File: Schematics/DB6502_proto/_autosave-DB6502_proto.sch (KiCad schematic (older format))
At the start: 13 parts, among them U1 74HC21, U2 74AC74, U3 65C02S, U4 22V10C, U5 74AC138, U6 74AC08

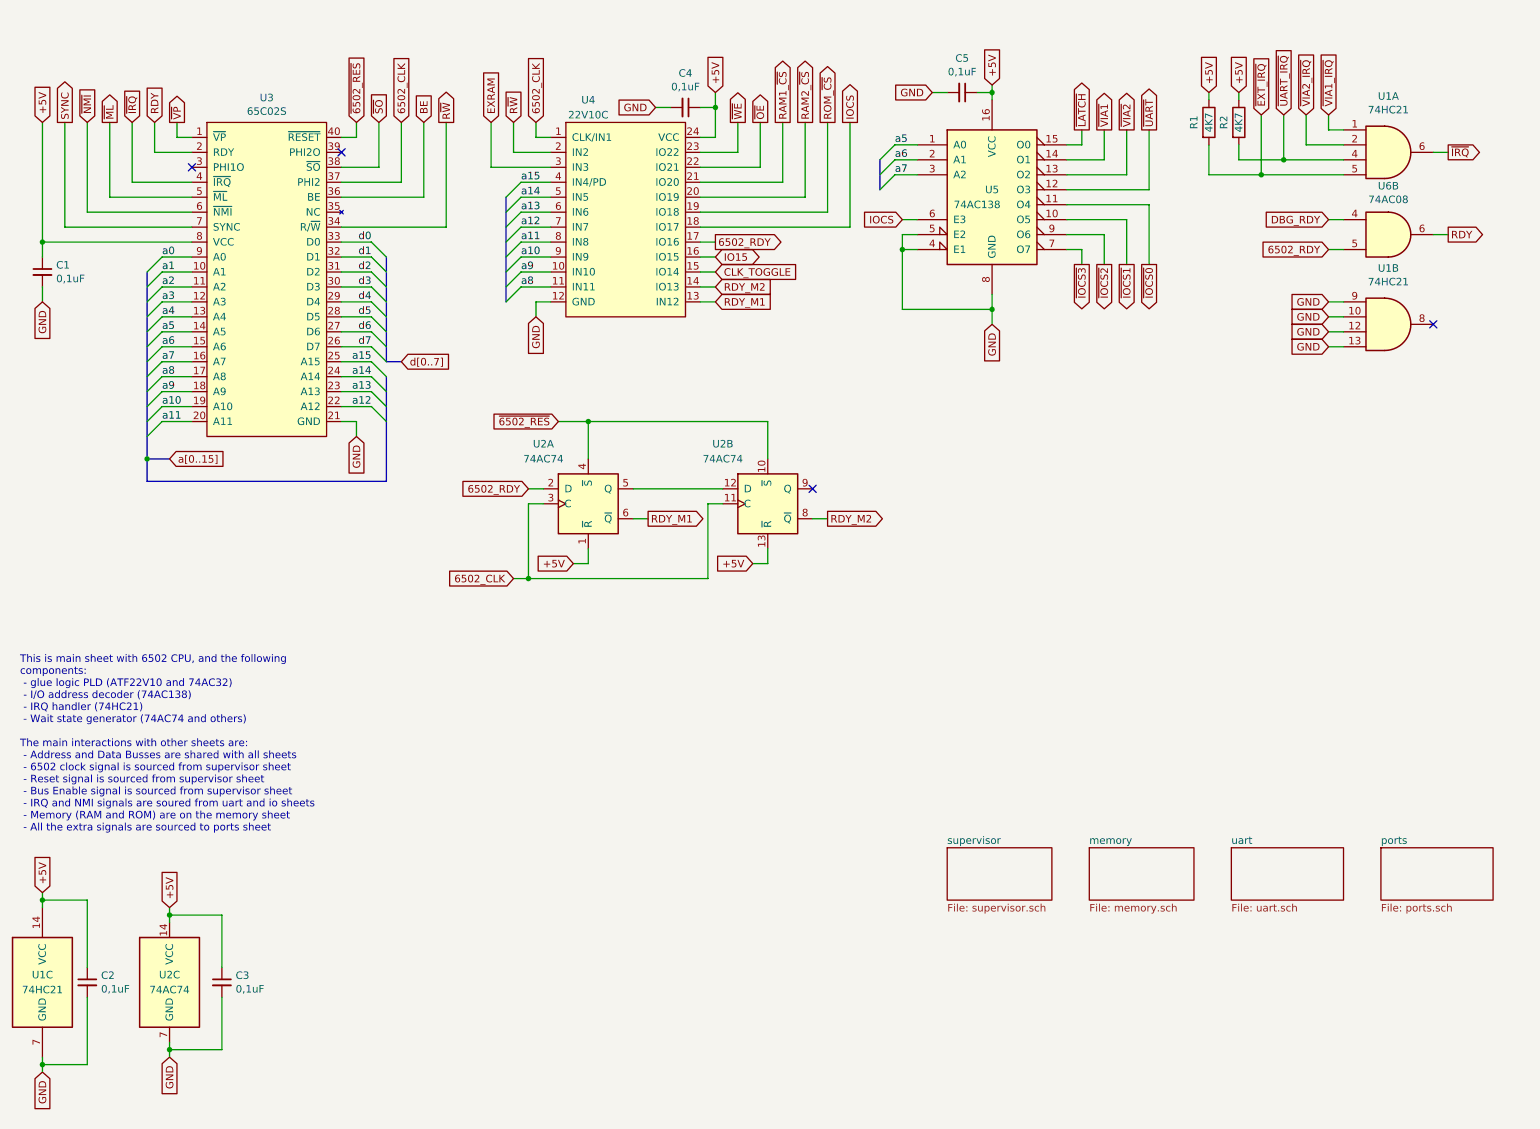
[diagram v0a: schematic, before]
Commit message: Updated schematic to reflect PLD WS generator
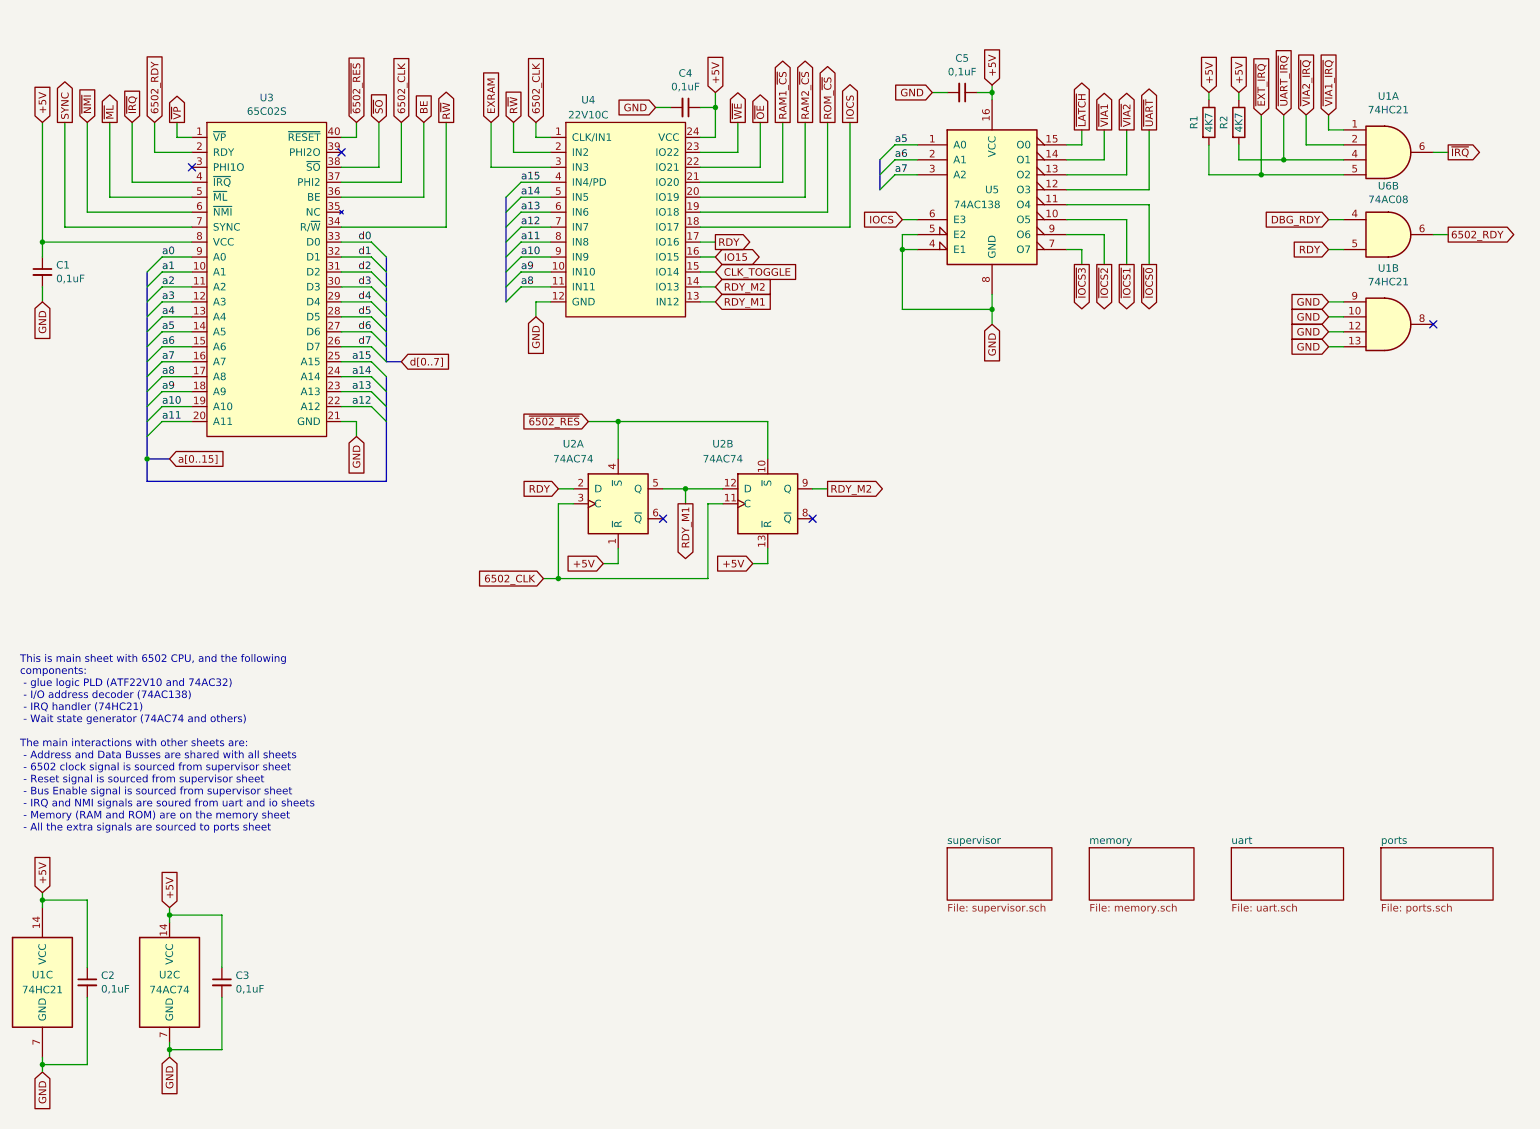
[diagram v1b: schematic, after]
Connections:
- net 6502_RDY: now also U3.2 (RDY), U6.6; no longer U2.2 (D), U4.17 (IO16), U6.5
- net RDY: now also U2.2 (D), U4.17 (IO16), U6.5; no longer U3.2 (RDY), U6.6
- net RDY_M1: now also U2.12 (D), U2.5 (Q); no longer U2.6 (~Q)
- net RDY_M2: now also U2.9 (Q); no longer U2.8 (~Q)
- no-connect marks 4 -> 5
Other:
- moved on the sheet: U2A
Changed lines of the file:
@@
 $EndDescr
 Text GLabel 1650 1150 1    50   Input ~ 0
-RDY
+6502_RDY
 NoConn ~ 1900 1450
 Text GLabel 1500 1150 1    50   Input ~ 0
@@
 IO15
 Text GLabel 5400 1950 2    50   Output ~ 0
-6502_RDY
+RDY
 Wire Wire Line
 	5300 1950 5400 1950
@@
 	9500 1800 9600 1800
 Text GLabel 10300 1900 2    50   Output ~ 0
-RDY
+6502_RDY
 $Comp
 L Device:C_Small C1
@@
 	10200 1900 10300 1900
 Text GLabel 9500 2000 0    50   Input ~ 0
-6502_RDY
+RDY
 Wire Wire Line
 	9500 2000 9600 2000
@@
 L 74xx:74HC74 U?
 U 1 1 5FA636F8
-P 4550 3700
+P 4750 3700
 AR Path="/5F8F4E1E/5FA636F8" Ref="U?"  Part="2"
 AR Path="/5FA636F8" Ref="U2"  Part="1"
-F 0 "U2" H 4250 4100 50  0000 C CNN
-F 1 "74AC74" H 4250 4000 50  0000 C CNN
-F 2 "Package_DIP:DIP-14_W7.62mm_Socket" H 4550 3700 50  0001 C CNN
-F 3 "74xx/74hc_hct74.pdf" H 4550 3700 50  0001 C CNN
-	1    4550 3700
-	1    0    0    -1
-$EndComp
-Text GLabel 4050 4200 0    50   Input ~ 0
+F 0 "U2" H 4450 4100 50  0000 C CNN
+F 1 "74AC74" H 4450 4000 50  0000 C CNN
+F 2 "Package_DIP:DIP-14_W7.62mm_Socket" H 4750 3700 50  0001 C CNN
+F 3 "74xx/74hc_hct74.pdf" H 4750 3700 50  0001 C CNN
+	1    4750 3700
+	1    0    0    -1
+$EndComp
+Text GLabel 4250 4200 0    50   Input ~ 0
 6502_CLK
-Text GLabel 4350 3150 0    50   Input ~ 0
+Text GLabel 4550 3150 0    50   Input ~ 0
 ~6502_RES
 Wire Wire Line
-	4350 3150 4550 3150
-Wire Wire Line
-	4550 3150 4550 3400
-Wire Wire Line
-	4550 3150 5750 3150
+	4550 3150 4750 3150
+Wire Wire Line
+	4750 3150 4750 3400
+Wire Wire Line
+	4750 3150 5750 3150
 Wire Wire Line
 	5750 3150 5750 3400
-Connection ~ 4550 3150
-Text GLabel 4450 4100 0    50   Input ~ 0
+Connection ~ 4750 3150
+Text GLabel 4650 4100 0    50   Input ~ 0
 +5V
 Wire Wire Line
-	4450 4100 4550 4100
-Wire Wire Line
-	4550 4100 4550 4000
+	4650 4100 4750 4100
+Wire Wire Line
+	4750 4100 4750 4000
 Text GLabel 5650 4100 0    50   Input ~ 0
 +5V
@@
 	5750 4100 5750 4000
 Wire Wire Line
-	4850 3600 5450 3600
-Wire Wire Line
-	4050 4200 4150 4200
-Wire Wire Line
-	4150 4200 4150 3700
-Wire Wire Line
-	4150 3700 4250 3700
-Wire Wire Line
-	4150 4200 5350 4200
+	5050 3600 5200 3600
+Wire Wire Line
+	4250 4200 4350 4200
+Wire Wire Line
+	4350 4200 4350 3700
+Wire Wire Line
+	4350 3700 4450 3700
+Wire Wire Line
+	4350 4200 5350 4200
 Wire Wire Line
 	5350 4200 5350 3700
 Wire Wire Line
 	5350 3700 5450 3700
-Connection ~ 4150 4200
-Text GLabel 4150 3600 0    50   Input ~ 0
-6502_RDY
-Wire Wire Line
-	4150 3600 4250 3600
-Text GLabel 6150 3800 2    50   Output ~ 0
+Connection ~ 4350 4200
+Text GLabel 4350 3600 0    50   Input ~ 0
+RDY
+Wire Wire Line
+	4350 3600 4450 3600
+Text GLabel 6150 3600 2    50   Output ~ 0
 RDY_M2
 Wire Wire Line
-	6050 3800 6150 3800
-Text GLabel 4950 3800 2    50   Output ~ 0
+	6050 3600 6150 3600
+Text GLabel 5200 3700 3    50   Output ~ 0
 RDY_M1
 Wire Wire Line
-	4850 3800 4950 3800
-NoConn ~ 6050 3600
+	5200 3600 5200 3700
+NoConn ~ 6050 3800
+Connection ~ 5200 3600
+Wire Wire Line
+	5200 3600 5450 3600
+NoConn ~ 5050 3800
 Wire Bus Line
 	6500 1400 6500 1600
